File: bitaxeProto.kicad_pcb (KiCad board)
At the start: 6 copper layers, 76 x 101 mm, 242 parts, among them J1 XT30, J2 Conn_01x03, J4 Conn_01x04, J5 Conn_01x10, J6 USB_C_Receptacle_USB2.0, Q1 BSS138, SW3 SWITCH-SPST, SW4 SWITCH-SPST, U1 MCP1824T-1202E/OT, U10 TPS82130, U11 RP2040, U12 ESP32-S3-WROOM-1, U2 TPS546D24SRVFR, U3 MCP1824T-1202E/OT, U4 MCP1824T-1202E/OT, U5 W25Q16JVUXIQ TR, U6 MCP1824T-1202E/OT, U7 TPS82130, U8 SN74AXC4T774, U9 TPS22919DCKR, Y1 12MHz, Y2 50MHz

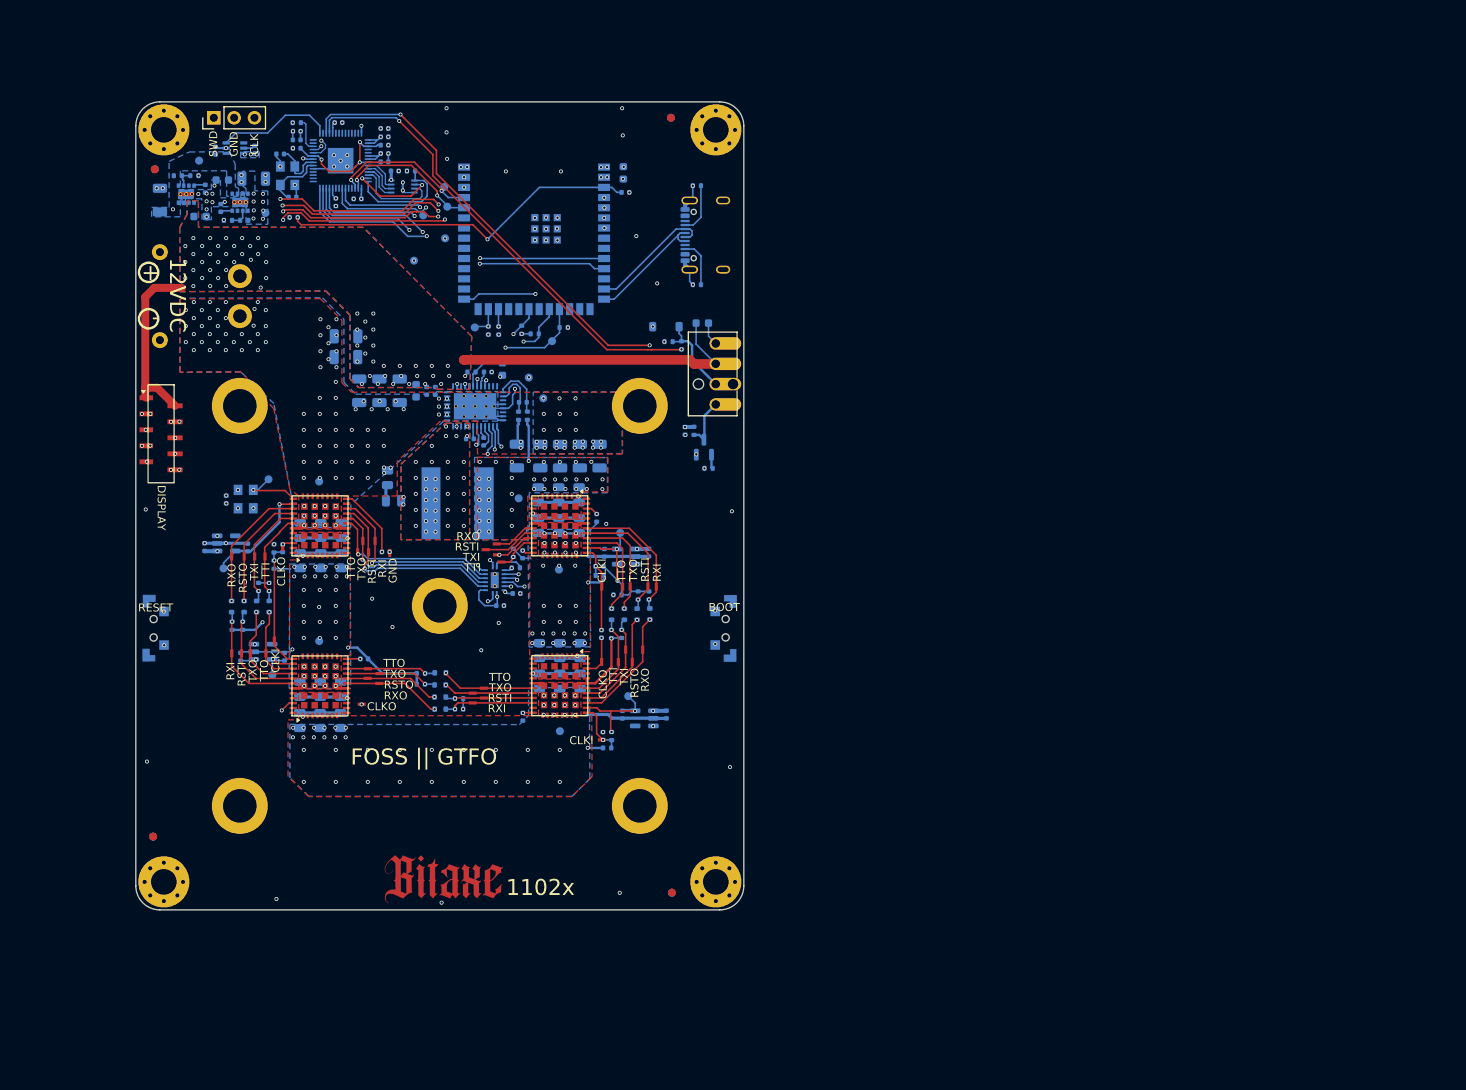
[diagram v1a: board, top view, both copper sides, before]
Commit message: add footprints and some 3d cad. rough part placements
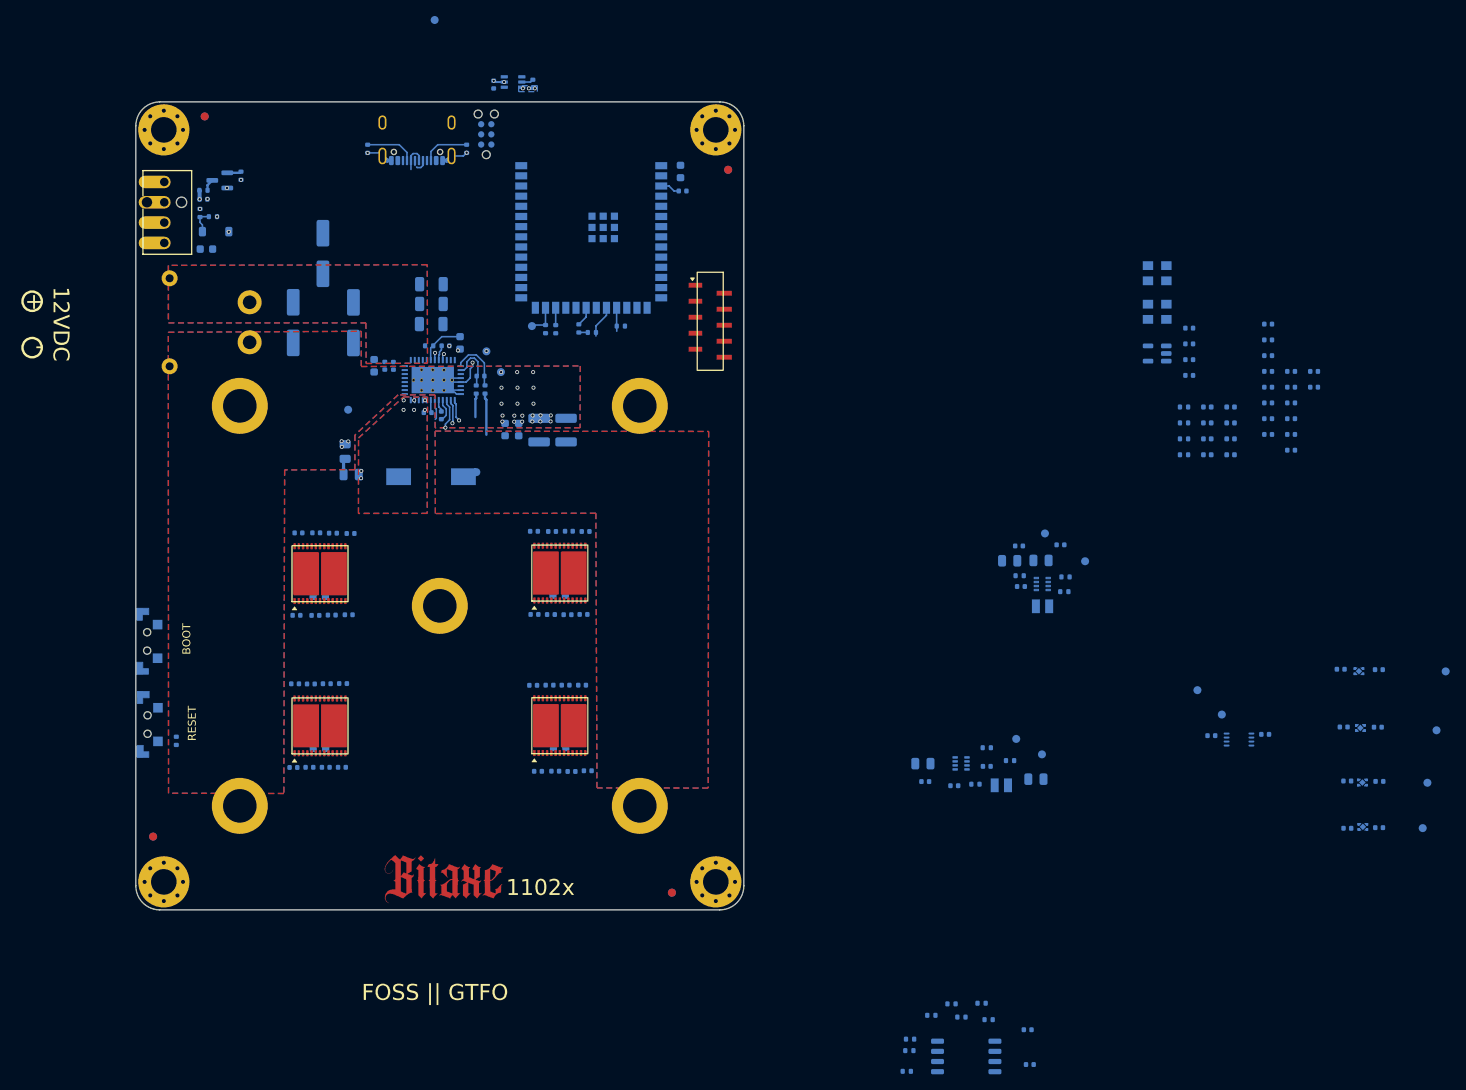
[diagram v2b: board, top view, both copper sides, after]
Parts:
- removed C132, C133, C139, C140, C141: 100uF, Capacitor_SMD:C_0805_2012Metric
- removed C142, C143, C144: 1000pF, Capacitor_SMD:C_0402_1005Metric
- removed C20: 47uF, Capacitor_SMD:C_1206_3216Metric
- removed C26, C27, C28, C39: 1uF, Capacitor_SMD:C_0402_1005Metric
- removed C31, C4, C5: 22uF, Capacitor_SMD:C_1206_3216Metric
- removed C32, C40, C43, C44, C45, C46, C58: 0.1uF, Capacitor_SMD:C_0402_1005Metric
- removed C33: 30pF, Capacitor_SMD:C_0402_1005Metric
- removed C60, C62, C63, C64: 120pF, Capacitor_SMD:C_0402_1005Metric
- removed D1, D10, D11, D12, D2, D3, D4, D5, D6, D7, D8, D9: DLLFSD01T-7, bitaxe:D_SOD-523
- removed J2: Conn_01x03, Connector_PinHeader_2.54mm:PinHeader_1x03_P2.54mm_Vertical
- removed R10: 536k, Resistor_SMD:R_0402_1005Metric
- removed R11: 100k, Resistor_SMD:R_0402_1005Metric
- removed R35, R36, R37, R38, R39, R4, R40, R41, R42, R43, R44, R45, R46, R47, R48, R49, R50, R51, R52: 1k, Resistor_SMD:R_0402_1005Metric
- removed R9: 10k, Resistor_SMD:R_0402_1005Metric
- removed TP14, TP31, TP38, TP46: RXO, bitaxe:TestPoint_Pad_1.0x0.4mm
- removed TP15: 5V, bitaxe:TestPoint_Pad_D1.0mm
- removed TP16: TXC, bitaxe:TestPoint_Pad_D1.0mm
- removed TP17, TP33, TP40, TP50, TP54: TXO, bitaxe:TestPoint_Pad_1.0x0.4mm
- removed TP18: 1V2-1, bitaxe:TestPoint_Pad_D1.0mm
- removed TP22: GND, bitaxe:TestPoint_Pad_1.0x0.4mm
- removed TP23: RXC, bitaxe:TestPoint_Pad_D1.0mm
- removed TP24: TXD, bitaxe:TestPoint_Pad_D1.0mm
- removed TP25: RXD, bitaxe:TestPoint_Pad_D1.0mm
- removed TP26: GND, bitaxe:TestPoint_Pad_D1.0mm
- removed TP28, TP43: TTI, bitaxe:TestPoint_Pad_1.0x0.4mm
- removed TP29, TP44: TXI, bitaxe:TestPoint_Pad_1.0x0.4mm
- removed TP3: 1V2-3, bitaxe:TestPoint_Pad_D1.0mm
- removed TP30, TP39, TP45: RSTO, bitaxe:TestPoint_Pad_1.0x0.4mm
- removed TP32, TP51, TP55: RSTI, bitaxe:TestPoint_Pad_1.0x0.4mm
- removed TP34, TP41, TP49, TP53: TTO, bitaxe:TestPoint_Pad_1.0x0.4mm
- removed TP35, TP48, TP57: CLKI, bitaxe:TestPoint_Pad_1.0x0.4mm
- removed TP36, TP52, TP56: RXI, bitaxe:TestPoint_Pad_1.0x0.4mm
- removed TP37, TP42, TP47: CLKO, bitaxe:TestPoint_Pad_1.0x0.4mm
- removed TP58: D1, bitaxe:TestPoint_Pad_D1.0mm
- removed TP59: D2, bitaxe:TestPoint_Pad_D1.0mm
- removed TP60: D3, bitaxe:TestPoint_Pad_D1.0mm
- removed U1, U6: MCP1824T-1202E/OT, bitaxe:SOT-23-5
- removed U10, U7: TPS82130, bitaxe:Texas_SIL0008D_MicroSiP-8-1EP_2.8x3mm_P0.65mm_EP1.1x1.9mm_ThermalVias
- removed U11: RP2040, bitaxe:RP2040-QFN-56-1EP_7x7mm_P0.4mm_EP3.2x3.2mm
- removed Y1: 12MHz, bitaxe:XTAL_ECS-120-20-33-CKM-TR3
- removed Y2: 50MHz, bitaxe:OSC_ECS-3225MV-500-CN-TR
- added C102: 1uF, Capacitor_SMD:C_0402_1005Metric, B.Cu at (118.9, 121.7)
- added C103: 1uF, Capacitor_SMD:C_0402_1005Metric, B.Cu at (116.9, 121.7)
- added C104: 1uF, Capacitor_SMD:C_0402_1005Metric, B.Cu at (114.9, 121.8)
- added C105: 1uF, Capacitor_SMD:C_0402_1005Metric, B.Cu at (112.9, 121.7)
- added C106: 1uF, Capacitor_SMD:C_0402_1005Metric, B.Cu at (142.7, 121.9)
- added C110: 1uF, Capacitor_SMD:C_0402_1005Metric, B.Cu at (143.3, 132.7)
- added C111: 1uF, Capacitor_SMD:C_0402_1005Metric, B.Cu at (145.4, 132.7)
- added C112: 1uF, Capacitor_SMD:C_0402_1005Metric, B.Cu at (147.5, 132.7)
- added C113: 1uF, Capacitor_SMD:C_0402_1005Metric, B.Cu at (149.5, 132.6)
- added C114: 1uF, Capacitor_SMD:C_0402_1005Metric, B.Cu at (113.3, 102.9)
- added C118: 1uF, Capacitor_SMD:C_0402_1005Metric, B.Cu at (113.1, 113.2)
- added C119: 1uF, Capacitor_SMD:C_0402_1005Metric, B.Cu at (115.5, 113.2)
- added C120: 1uF, Capacitor_SMD:C_0402_1005Metric, B.Cu at (117.5, 113.2)
- added C121: 1uF, Capacitor_SMD:C_0402_1005Metric, B.Cu at (119.6, 113.1)
- added C122: 1uF, Capacitor_SMD:C_0402_1005Metric, B.Cu at (142.8, 102.7)
- added C126: 1uF, Capacitor_SMD:C_0402_1005Metric, B.Cu at (142.8, 113.1)
- added C127: 1uF, Capacitor_SMD:C_0402_1005Metric, B.Cu at (144.9, 113.1)
- added C128: 1uF, Capacitor_SMD:C_0402_1005Metric, B.Cu at (147.0, 113.1)
- added C129: 1uF, Capacitor_SMD:C_0402_1005Metric, B.Cu at (149.0, 113.1)
- added C130: 0.1uF, Capacitor_SMD:C_0402_1005Metric, B.Cu at (224.7, 77.3)
- added C206: 0.1uF, Capacitor_SMD:C_0402_1005Metric, B.Cu at (204.5, 165.0)
- added C207: 1uF, Capacitor_SMD:C_0402_1005Metric, B.Cu at (204.8, 169.3)
- added C208: 0.1uF, Capacitor_SMD:C_0402_1005Metric, B.Cu at (224.7, 81.2)
- added C209: 1uF, Capacitor_SMD:C_0402_1005Metric, B.Cu at (224.7, 83.2)
- added C49: 1uF, Capacitor_SMD:C_0402_1005Metric, B.Cu at (244.0, 127.1)
- added C50: 1uF, Capacitor_SMD:C_0402_1005Metric, B.Cu at (248.4, 120.0)
- added C51: 0.1uF, Capacitor_SMD:C_0402_1005Metric, B.Cu at (240.3, 82.7)
- added C52: 0.1uF, Capacitor_SMD:C_0402_1005Metric, B.Cu at (240.3, 84.7)
- added C53: 1uF, Capacitor_SMD:C_0402_1005Metric, B.Cu at (244.4, 133.9)
- added C54: 1uF, Capacitor_SMD:C_0402_1005Metric, B.Cu at (244.4, 139.8)
- added C55: 1uF, Capacitor_SMD:C_0402_1005Metric, B.Cu at (248.2, 127.2)
- added C56: 1uF, Capacitor_SMD:C_0402_1005Metric, B.Cu at (248.4, 133.9)
- added C66: 10uF, Capacitor_SMD:C_0603_1608Metric, B.Cu at (146.0, 125.0)
- added C67: 10uF, Capacitor_SMD:C_0603_1608Metric, B.Cu at (146.0, 126.6)
- added C69: 10uF, Capacitor_SMD:C_0603_1608Metric, B.Cu at (146.0, 129.7)
- added C70: 10uF, Capacitor_SMD:C_0603_1608Metric, B.Cu at (146.0, 105.9)
- added C71: 10uF, Capacitor_SMD:C_0603_1608Metric, B.Cu at (146.0, 107.5)
- added C73: 10uF, Capacitor_SMD:C_0603_1608Metric, B.Cu at (116.0, 125.1)
- added C74: 10uF, Capacitor_SMD:C_0603_1608Metric, B.Cu at (116.0, 126.7)
- added C75: 10uF, Capacitor_SMD:C_0603_1608Metric, B.Cu at (116.0, 128.2)
- added C78: 10uF, Capacitor_SMD:C_0603_1608Metric, B.Cu at (116.0, 129.8)
- added C79: 4.7uF, Capacitor_SMD:C_0402_1005Metric, B.Cu at (237.4, 84.7)
- added C80: 10uF, Capacitor_SMD:C_0603_1608Metric, B.Cu at (116.0, 106.0)
- added C81: 10uF, Capacitor_SMD:C_0603_1608Metric, B.Cu at (116.0, 107.6)
- added C82: 10uF, Capacitor_SMD:C_0603_1608Metric, B.Cu at (116.0, 109.2)
- added C86: 0.1uF, Capacitor_SMD:C_0402_1005Metric, B.Cu at (237.4, 90.6)
- added C87: 4.7uF, Capacitor_SMD:C_0402_1005Metric, B.Cu at (237.4, 92.5)
- added C88: 0.1uF, Capacitor_SMD:C_0402_1005Metric, B.Cu at (234.5, 76.8)
- added C89: 4.7uF, Capacitor_SMD:C_0402_1005Metric, B.Cu at (234.5, 78.8)
- added C90: 0.1uF, Capacitor_SMD:C_0402_1005Metric, B.Cu at (234.5, 80.7)
- added C94: 4.7uF, Capacitor_SMD:C_0402_1005Metric, B.Cu at (234.5, 86.6)
- added C95: 10uF, Capacitor_SMD:C_0603_1608Metric, B.Cu at (145.9, 110.7)
- added C96: 0.1uF, Capacitor_SMD:C_0402_1005Metric, B.Cu at (234.5, 88.6)
- added C97: 4.7uF, Capacitor_SMD:C_0402_1005Metric, B.Cu at (234.5, 90.6)
- added C98: 1uF, Capacitor_SMD:C_0402_1005Metric, B.Cu at (112.7, 132.2)
- added FB10: FerriteBead_Small, Inductor_SMD:L_0402_1005Metric, B.Cu at (226.9, 93.1)
- added FB3: FerriteBead_Small, Inductor_SMD:L_0402_1005Metric, B.Cu at (229.8, 87.1)
- added FB4: FerriteBead_Small, Inductor_SMD:L_0402_1005Metric, B.Cu at (229.8, 89.1)
- added FB5: FerriteBead_Small, Inductor_SMD:L_0402_1005Metric, B.Cu at (229.8, 91.1)
- added FB6: FerriteBead_Small, Inductor_SMD:L_0402_1005Metric, B.Cu at (229.8, 93.1)
- added FB7: FerriteBead_Small, Inductor_SMD:L_0402_1005Metric, B.Cu at (226.9, 87.1)
- added FB8: FerriteBead_Small, Inductor_SMD:L_0402_1005Metric, B.Cu at (226.9, 89.1)
- added FB9: FerriteBead_Small, Inductor_SMD:L_0402_1005Metric, B.Cu at (226.9, 91.1)
- added J8: TC2030-IDC, Connector:Tag-Connect_TC2030-IDC-NL_2x03_P1.27mm_Vertical, B.Cu at (136.8, 53.1)
- added L2: 1.5uH, bitaxe:IND-SMD_L2.0-W1.6, B.Cu at (206.3, 112.0)
- added L3: 1.5uH, bitaxe:IND-SMD_L2.0-W1.6, B.Cu at (201.2, 134.4)
- added R15: 10k, Resistor_SMD:R_0402_1005Metric, B.Cu at (197.9, 134.3)
- added R25: 10k, Resistor_SMD:R_0402_1005Metric, B.Cu at (224.0, 87.1)
- added R27: 10k, Resistor_SMD:R_0402_1005Metric, B.Cu at (202.3, 131.3)
- added R55: 1k, Resistor_SMD:R_0402_1005Metric, B.Cu at (198.7, 161.7)
- added R56: 10k, Resistor_SMD:R_0402_1005Metric, B.Cu at (195.0, 161.8)
- added R57: 10k, Resistor_SMD:R_0402_1005Metric, B.Cu at (192.4, 163.2)
- added R58: 1k, Resistor_SMD:R_0402_1005Metric, B.Cu at (189.4, 170.2)
- added R59: 10k, Resistor_SMD:R_0402_1005Metric, B.Cu at (189.7, 167.6)
- added R60: 10k, Resistor_SMD:R_0402_1005Metric, B.Cu at (189.8, 166.2)
- added R68: 1k, Resistor_SMD:R_0402_1005Metric, B.Cu at (199.6, 163.7)
- added R69: 1k, Resistor_SMD:R_0402_1005Metric, B.Cu at (196.2, 163.4)
- added R70: 220k, Resistor_SMD:R_0402_1005Metric, B.Cu at (224.0, 91.1)
- added R71: 1k, Resistor_SMD:R_0402_1005Metric, B.Cu at (224.0, 93.1)
- added U13: TS3011, bitaxe:SOT-23-5, B.Cu at (220.7, 80.5)
- added U14: SN74AVC2T45DCUR, bitaxe:VSSOP-8_L2.1-W2.4-P0.50-LS3.2-BR, B.Cu at (230.9, 128.7)
- added U15: 25MHz, bitaxe:SMD3225-4P, B.Cu at (220.7, 75.2)
- added U16: TLV75512PDQNR, bitaxe:DQN0004A, B.Cu at (246.1, 127.3)
- added U17: TLV755075PDQNR, bitaxe:DQN0004A, B.Cu at (246.3, 134.1)
- added U18: TLV75512PDQNR, bitaxe:DQN0004A, B.Cu at (246.4, 139.6)
- added U19: TLV3542, Package_SO:SOIC-8_5.3x5.3mm_P1.27mm, B.Cu at (196.8, 168.3)
- A1, A3: value BZM2_MODE0 -> ProtoMC3; footprint bitaxe:bzm2 -> bitaxe:proto-mc3
- A2, A4: value BZM2_MODE1 -> ProtoMC3; footprint bitaxe:bzm2 -> bitaxe:proto-mc3
- C1: value 10uF -> 68uF; footprint Capacitor_SMD:C_0603_1608Metric -> Capacitor_SMD:C_Elec_6.3x7.7
- C100, C101, C107, C108, C109, C115, C116, C117, C123, C124, C125, C99: value 100uF -> 1uF; footprint Capacitor_SMD:C_0805_2012Metric -> Capacitor_SMD:C_0402_1005Metric
- C12: value 3.3nF -> 10uF; footprint Capacitor_SMD:C_0402_1005Metric -> Capacitor_SMD:C_0805_2012Metric
- C131, C85, C92: value 100uF -> 4.7uF; footprint Capacitor_SMD:C_0805_2012Metric -> Capacitor_SMD:C_0402_1005Metric
- C19, C7: value 1uF -> 4.7uF; footprint Capacitor_SMD:C_0402_1005Metric -> Capacitor_SMD:C_1206_3216Metric
- C2, C3: value 22uF -> 68uF; footprint Capacitor_SMD:C_1206_3216Metric -> Capacitor_SMD:C_Elec_6.3x7.7
- C21, C22: value 100uF -> 22uF; footprint Capacitor_SMD:C_1206_3216Metric -> Capacitor_SMD:C_0603_1608Metric
- C23, C24: footprint Capacitor_SMD:C_1206_3216Metric -> Capacitor_SMD:C_1210_3225Metric
- C29: value 3.3nF -> 33nF
- C30: value 22uF -> 33nF; footprint Capacitor_SMD:C_1206_3216Metric -> Capacitor_SMD:C_0402_1005Metric
- C35: value 30pF -> 22uF; footprint Capacitor_SMD:C_0402_1005Metric -> Capacitor_SMD:C_0805_2012Metric
- C36: value 0.1uF -> 22uF; footprint Capacitor_SMD:C_0402_1005Metric -> Capacitor_SMD:C_0805_2012Metric
- C38, C72: value 1uF -> 0.1uF
- C57: value 0.1uF -> 1uF
- C6: value 22uF -> 4.7uF
- C61: value 120pF -> 0.1uF
- C68: value 1uF -> 10uF; footprint Capacitor_SMD:C_0402_1005Metric -> Capacitor_SMD:C_0603_1608Metric
- C8: footprint Capacitor_SMD:C_0603_1608Metric -> Capacitor_SMD:C_0805_2012Metric
- C83, C93: value 100uF -> 10uF; footprint Capacitor_SMD:C_0805_2012Metric -> Capacitor_SMD:C_0603_1608Metric
- C84, C91: value 100uF -> 0.1uF; footprint Capacitor_SMD:C_0805_2012Metric -> Capacitor_SMD:C_0402_1005Metric
- L1: value 1.2uH -> 230nH; footprint bitaxe:XAL1060122MEC -> bitaxe:IND-SMD_L11.0-W7.2
- R12: value 309k -> 30.9k
- R13: value 100k -> 10k
- R14: value 10k -> 13.7k
- R16: value 49.9k -> 52.3k
- R26: value 20k -> 12k
- TP11: value TTI -> CLKI; footprint bitaxe:TestPoint_Pad_1.0x0.4mm -> bitaxe:TestPoint_Pad_D1.0mm; moved to B.Cu
- TP12: value TXI -> 1V2; footprint bitaxe:TestPoint_Pad_1.0x0.4mm -> bitaxe:TestPoint_Pad_D1.0mm; moved to B.Cu
- TP13: value RSTI -> 5V; footprint bitaxe:TestPoint_Pad_1.0x0.4mm -> bitaxe:TestPoint_Pad_D1.0mm; moved to B.Cu
- TP2: value 1V2-2 -> 0V75-0
- TP20: value RXI -> GND; footprint bitaxe:TestPoint_Pad_1.0x0.4mm -> bitaxe:TestPoint_Pad_D1.0mm; moved to B.Cu
- TP21: value TTO -> GND; footprint bitaxe:TestPoint_Pad_1.0x0.4mm -> bitaxe:TestPoint_Pad_D1.0mm; moved to B.Cu
- TP4: value 1V2-4 -> 1V2-0
- TP5, TP8: footprint TestPoint:TestPoint_Pad_D1.0mm -> bitaxe:TestPoint_Pad_D1.0mm
- TP6: value RSTI -> 0V75; footprint bitaxe:TestPoint_Pad_1.0x0.4mm -> bitaxe:TestPoint_Pad_D1.0mm; moved to B.Cu
- U3: value MCP1824T-1202E/OT -> TLV755075PDQNR; footprint bitaxe:SOT-23-5 -> bitaxe:DQN0004A
- U4: value MCP1824T-1202E/OT -> TPS62933DRLR; footprint bitaxe:SOT-23-5 -> bitaxe:SOT-583-8_L2.1-W1.2-P0.50-LS1.6-BR
- U5: value W25Q16JVUXIQ TR -> TPS62933DRLR; footprint bitaxe:USON-8_UX_2x3x0p6_WIN -> bitaxe:SOT-583-8_L2.1-W1.2-P0.50-LS1.6-BR
- U8: value SN74AXC4T774 -> 25MHz; footprint bitaxe:BQB0016A-MFG -> bitaxe:SMD3225-4P
- moved TP2 146.7 mm to (256.7, 120.2), turned to 180 degrees
- moved TP6 135.5 mm to (254.4, 134.1), turned to 180 degrees
- moved C72 132.3 mm to (237.4, 82.7), turned to 180 degrees
- moved C30 123.4 mm to (195.3, 134.5), turned to 180 degrees
- moved C84 122.9 mm to (237.4, 86.6), turned to 180 degrees
- moved TP10 122.7 mm to (228.8, 125.6), turned to 180 degrees
- moved C91 122.6 mm to (234.5, 82.7), turned to 180 degrees
- moved TP12 120.6 mm to (253.9, 139.8), turned to 180 degrees
- moved C85 120.0 mm to (237.4, 88.6), turned to 180 degrees
- moved C92 119.8 mm to (234.5, 84.7), turned to 180 degrees
- moved C42 117.2 mm to (199.4, 132.1), turned to 180 degrees
- moved R16 116.4 mm to (199.4, 129.7)
- moved C12 114.9 mm to (191.4, 131.7), turned to 180 degrees
- moved R13 114.4 mm to (209.1, 110.2), turned to 180 degrees
- moved C57 113.3 mm to (248.4, 139.7), turned to 180 degrees
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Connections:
- A1 pad 1: /ASIC/bypass1-1/out -> Net-(A1-CLKO)
- A1 pad 10: unconnected-(A1-TDI-Pad10) -> GND
- A1 pad 11: unconnected-(A1-TCK-Pad11) -> Net-(A1-VDDI1_0)
- A1 pad 12: /ASIC/bypass1-2/in -> Net-(A1-VDDI2_0)
- A1 pad 13: unconnected-(A1-RSVD-Pad13) -> Net-(A1-VDDI3_0)
- A1 pad 14: GND -> Net-(A1-VDDI3_1)
- A1 pad 15: /ASIC/TRIP_1V2 -> Net-(A1-VDDI2_1)
- A1 pad 16: /ASIC/TX_1V2 -> Net-(A1-VDDI1_1)
- A1 pad 17: /ASIC/RST_1V2 -> GND
- A1 pad 18: /ASIC/RX_1V2 -> unconnected-(A1-VEFS-Pad18)
- A1 pad 19: unconnected-(A1-VDDIO-Pad19) -> /ASIC/RST_1V2
- A1 pad 2: /ASIC/GND2 -> unconnected-(A1-UTXN-Pad2)
- A1 pad 20: Net-(A1-REFCLKOUT2) -> unconnected-(A1-TO-Pad20)
- A1 pad 21: GND -> Net-(A1-VDDIO12-Pad21)
- A1 pad 22: GND -> Net-(A1-VDDH-Pad22)
- A1 pad 24: GND -> /ASIC/RX_1V2
- A1 pad 25: GND -> unconnected-(A1-URXN-Pad25)
- A1 pad 26: GND -> /ASIC/CLKI
- A1 pad 28: GND -> /ASIC/GND0
- A1 pad 3: /ASIC/GND2 -> Net-(A1-UTXP)
- A1 pad 4: /ASIC/GND2 -> unconnected-(A1-ATEST-Pad4)
- A1 pad 5: /ASIC/GND2 -> Net-(A1-VDDH-Pad22)
- A1 pad 6: /ASIC/GND2 -> Net-(A1-VDDIO12-Pad21)
- A1 pad 7: /ASIC/GND2 -> Net-(A1-nRST-Pad7)
- A1 pad 8: /ASIC/GND2 -> GND
- A1 pad 9: unconnected-(A1-TDO-Pad9) -> GND
- A2 pad 1: /ASIC/bypass2-1/out -> unconnected-(A2-CLKO-Pad1)
- A2 pad 10: unconnected-(A2-TDI-Pad10) -> GND
- A2 pad 11: unconnected-(A2-TCK-Pad11) -> Net-(A2-VDDI1_0)
- A2 pad 12: /ASIC/bypass2-2/in -> Net-(A2-VDDI2_0)
- A2 pad 13: unconnected-(A2-RSVD-Pad13) -> Net-(A2-VDDI3_0)
- A2 pad 14: /ASIC/GND2 -> Net-(A2-VDDI3_1)
- A2 pad 15: /ASIC/shifter2-3/RX_OUT -> Net-(A2-VDDI2_1)
- A2 pad 16: /ASIC/shifter2-3/RESET_OUT -> Net-(A2-VDDI1_1)
- A2 pad 17: /ASIC/shifter2-3/TX_IN -> GND
- A2 pad 18: /ASIC/shifter2-3/TRIP_IN -> unconnected-(A2-VEFS-Pad18)
- A2 pad 19: unconnected-(A2-VDDIO-Pad19) -> Net-(A1-nRST-Pad7)
- A2 pad 2: /ASIC/GND3 -> unconnected-(A2-UTXN-Pad2)
- A2 pad 20: Net-(A2-REFCLKOUT2) -> unconnected-(A2-TO-Pad20)
- A2 pad 21: /ASIC/GND2 -> /ASIC/1V2
- A2 pad 22: /ASIC/GND2 -> /ASIC/0V75
- A2 pad 23: /ASIC/GND2 -> GND
- A2 pad 24: /ASIC/GND2 -> Net-(A1-UTXP)
- A2 pad 25: /ASIC/GND2 -> unconnected-(A2-URXN-Pad25)
- A2 pad 26: /ASIC/GND2 -> Net-(A1-CLKO)
- A2 pad 27: /ASIC/GND2 -> GND
- A2 pad 28: /ASIC/GND2 -> /ASIC/GND0
- A2 pad 3: /ASIC/GND3 -> /ASIC/Level Shifter/TX_IN
- A2 pad 4: /ASIC/GND3 -> unconnected-(A2-ATEST-Pad4)
- A2 pad 5: /ASIC/GND3 -> /ASIC/0V75
- A2 pad 6: /ASIC/GND3 -> /ASIC/1V2
- A2 pad 7: /ASIC/GND3 -> /ASIC/Level Shifter/RST_IN
- A2 pad 8: /ASIC/GND3 -> GND
- A2 pad 9: unconnected-(A2-TDO-Pad9) -> GND
- A3 pad 1: /ASIC/bypass3-1/out -> /ASIC/CLKI-0
- A3 pad 10: unconnected-(A3-TDI-Pad10) -> /ASIC/GND0
- A3 pad 11: unconnected-(A3-TCK-Pad11) -> Net-(A3-VDDI1_0)
- A3 pad 12: /ASIC/bypass3-2/in -> Net-(A3-VDDI2_0)
- A3 pad 13: unconnected-(A3-RSVD-Pad13) -> Net-(A3-VDDI3_0)
- A3 pad 14: /ASIC/GND3 -> Net-(A3-VDDI3_1)
- A3 pad 15: /ASIC/shifter2-3/TRIP_OUT -> Net-(A3-VDDI2_1)
- A3 pad 16: /ASIC/shifter2-3/TX_OUT -> Net-(A3-VDDI1_1)
- A3 pad 17: /ASIC/shifter2-3/RESET_IN -> /ASIC/GND0
- A3 pad 18: /ASIC/shifter2-3/RX_IN -> unconnected-(A3-VEFS-Pad18)
- A3 pad 19: unconnected-(A3-VDDIO-Pad19) -> Net-(A3-nRST-Pad19)
- A3 pad 2: /ASIC/GND4 -> unconnected-(A3-URXN-Pad2)
- A3 pad 20: Net-(A3-REFCLKOUT2) -> unconnected-(A3-TO-Pad20)
- A3 pad 21: /ASIC/GND3 -> /ASIC/1V2-0
- A3 pad 22: /ASIC/GND3 -> /ASIC/0V75-0
- A3 pad 23: /ASIC/GND3 -> /ASIC/GND0
- A3 pad 24: /ASIC/GND3 -> Net-(A3-UTXP)
- A3 pad 25: /ASIC/GND3 -> unconnected-(A3-UTXN-Pad25)
- A3 pad 26: /ASIC/GND3 -> Net-(A3-CLKO)
- A3 pad 27: /ASIC/GND3 -> /ASIC/GND0
- A3 pad 28: /ASIC/GND3 -> /VDD
- A3 pad 3: /ASIC/GND4 -> /ASIC/Level Shifter/TX_OUT
- A3 pad 4: /ASIC/GND4 -> unconnected-(A3-ATEST-Pad4)
- A3 pad 5: /ASIC/GND4 -> /ASIC/0V75-0
- A3 pad 6: /ASIC/GND4 -> /ASIC/1V2-0
- A3 pad 7: /ASIC/GND4 -> /ASIC/Level Shifter/RST_OUT
- A3 pad 8: /ASIC/GND4 -> /ASIC/1V2-0
- A3 pad 9: unconnected-(A3-TDO-Pad9) -> /ASIC/GND0
- A4 pad 1: /ASIC/bypass4-1/out -> Net-(A3-CLKO)
- A4 pad 10: unconnected-(A4-TDI-Pad10) -> /ASIC/GND0
- A4 pad 11: unconnected-(A4-TCK-Pad11) -> Net-(A4-VDDI1_0)
- A4 pad 12: /ASIC/bypass4-2/in -> Net-(A4-VDDI2_0)
- A4 pad 13: unconnected-(A4-RSVD-Pad13) -> Net-(A4-VDDI3_0)
- A4 pad 14: /ASIC/GND4 -> Net-(A4-VDDI3_1)
- A4 pad 15: Net-(A4-RX_OUT) -> Net-(A4-VDDI2_1)
- A4 pad 16: Net-(A4-RESET_OUT) -> Net-(A4-VDDI1_1)
- A4 pad 17: Net-(A4-TX_IN) -> /ASIC/GND0
- A4 pad 18: Net-(A4-TRIP_IN) -> unconnected-(A4-VEFS-Pad18)
- A4 pad 2: /VDD -> unconnected-(A4-URXN-Pad2)
- A4 pad 20: Net-(A4-REFCLKOUT2) -> unconnected-(A4-TO-Pad20)
- A4 pad 21: /ASIC/GND4 -> Net-(A4-VDDIO12-Pad21)
- A4 pad 22: /ASIC/GND4 -> Net-(A4-VDDH-Pad22)
- A4 pad 23: /ASIC/GND4 -> /ASIC/GND0
- A4 pad 24: /ASIC/GND4 -> /ASIC/TX_2V4
- A4 pad 25: /ASIC/GND4 -> unconnected-(A4-UTXN-Pad25)
- A4 pad 26: /ASIC/GND4 -> unconnected-(A4-CLKO-Pad26)
- A4 pad 27: /ASIC/GND4 -> /ASIC/GND0
- A4 pad 28: /ASIC/GND4 -> /VDD
- A4 pad 3: /VDD -> Net-(A3-UTXP)
- A4 pad 4: /VDD -> unconnected-(A4-ATEST-Pad4)
- A4 pad 5: /VDD -> Net-(A4-VDDH-Pad22)
- A4 pad 6: /VDD -> Net-(A4-VDDIO12-Pad21)
- A4 pad 7: /VDD -> Net-(A3-nRST-Pad19)
- A4 pad 8: /VDD -> /ASIC/1V2-0
- A4 pad 9: unconnected-(A4-TDO-Pad9) -> /ASIC/GND0
- C1 pad 1: GND -> /12V
- C1 pad 2: /12V -> GND
- C100 pad 1: /ASIC/bypass2-1/out -> Net-(A2-VDDI2_0)
- C100 pad 2: /ASIC/GND3 -> Net-(A2-VDDI1_0)
- C101 pad 1: /ASIC/bypass2-1/out -> Net-(A2-VDDI1_0)
- C101 pad 2: /ASIC/GND3 -> GND
- C107 pad 1: /ASIC/GND2 -> Net-(A3-VDDI2_1)
- C107 pad 2: /ASIC/bypass2-2/in -> Net-(A3-VDDI1_1)
- C108 pad 1: /ASIC/GND2 -> Net-(A3-VDDI3_1)
- C108 pad 2: /ASIC/bypass2-2/in -> Net-(A3-VDDI2_1)
- C109 pad 1: /ASIC/GND2 -> /VDD
- C109 pad 2: /ASIC/bypass2-2/in -> Net-(A3-VDDI3_1)
- C115 pad 1: /ASIC/bypass3-1/out -> Net-(A1-VDDI2_1)
- C115 pad 2: /ASIC/GND4 -> Net-(A1-VDDI1_1)
- C116 pad 1: /ASIC/bypass3-1/out -> Net-(A1-VDDI3_1)
- C116 pad 2: /ASIC/GND4 -> Net-(A1-VDDI2_1)
- C117 pad 1: /ASIC/bypass3-1/out -> /ASIC/GND0
- C117 pad 2: /ASIC/GND4 -> Net-(A1-VDDI3_1)
- C12 pad 2: Net-(U7-SS/TR) -> /12V
- C123 pad 1: /ASIC/GND3 -> Net-(A4-VDDI2_1)
- C123 pad 2: /ASIC/bypass3-2/in -> Net-(A4-VDDI1_1)
- C124 pad 1: /ASIC/GND3 -> Net-(A4-VDDI3_1)
- C124 pad 2: /ASIC/bypass3-2/in -> Net-(A4-VDDI2_1)
- C125 pad 1: /ASIC/GND3 -> /VDD
- C125 pad 2: /ASIC/bypass3-2/in -> Net-(A4-VDDI3_1)
- C131 pad 1: /ASIC/bypass4-1/out -> /ASIC/GND0
- C131 pad 2: /VDD -> /ASIC/1V2-0
- C19 pad 1: /ASIC/GND2 -> /12V
- C19 pad 2: /ASIC/1V2-2 -> GND
- C25 pad 1: /ASIC/GND3 -> /ASIC/GND0
- C29 pad 2: Net-(U10-SS/TR) -> Net-(U4-SS)
- C30 pad 2: /5V -> Net-(U5-SS)
- C35 pad 2: /Data/XIN -> /3V3
- C36 pad 2: /Data/1V1 -> /5V
- C37 pad 1: GND -> /12V
- C37 pad 2: /Data/1V1 -> GND
- C38 pad 1: GND -> /12V
- C38 pad 2: /Data/1V1 -> GND
- C41 pad 1: GND -> Net-(U4-BST)
- C41 pad 2: /3V3 -> Net-(U4-SW)
- C42 pad 1: GND -> Net-(U5-BST)
- C42 pad 2: /3V3 -> Net-(U5-SW)
- C57 pad 1: /ASIC/1V2-1 -> GND
- C57 pad 2: GND -> /ASIC/1V2
- C59 pad 1: /3V3 -> /ASIC/1V2
- C59 pad 2: GND -> Net-(U14-GND)
- C61 pad 1: Net-(A4-REFCLKOUT2) -> /3V3
- C61 pad 2: /ASIC/GND4 -> Net-(U14-GND)
- C68 pad 1: GND -> /VDD
- C68 pad 2: /5V_SWITCH -> /ASIC/GND0
- C7 pad 1: /ASIC/GND2 -> /12V
- C7 pad 2: /5V_SWITCH -> GND
- C72 pad 2: /ASIC/1V2-1 -> /ASIC/0V75
- C8 pad 2: /5V -> /12V
- C83 pad 1: /ASIC/bypass1-1/out -> /ASIC/GND0
- C83 pad 2: /ASIC/GND2 -> GND
- C84 pad 1: /ASIC/bypass1-1/out -> GND
- C84 pad 2: /ASIC/GND2 -> /ASIC/0V75
- C85 pad 1: /ASIC/bypass1-1/out -> GND
- C85 pad 2: /ASIC/GND2 -> /ASIC/0V75
- C91 pad 2: /ASIC/bypass1-2/in -> /ASIC/1V2
- C92 pad 1: GND -> /ASIC/GND0
- C92 pad 2: /ASIC/bypass1-2/in -> /ASIC/1V2-0
- C93 pad 1: GND -> /VDD
- C93 pad 2: /ASIC/bypass1-2/in -> /ASIC/GND0
- C99 pad 1: /ASIC/bypass2-1/out -> Net-(A2-VDDI3_0)
- C99 pad 2: /ASIC/GND3 -> Net-(A2-VDDI2_0)
- R12 pad 1: Net-(U10-FB) -> Net-(U4-FB)
- R13 pad 2: Net-(U10-FB) -> Net-(U4-FB)
- R14 pad 1: /3V3 -> GND
- R14 pad 2: /Data/QSPI_SS -> Net-(U4-RT)
- R16 pad 1: Net-(U11-RUN) -> Net-(U5-FB)
- R16 pad 2: /3V3 -> /5V
- R26 pad 2: Net-(U8-OE) -> Net-(U13--)
- TP10 pad 1: /ASIC/REFCLKIN1 -> /ASIC/CLKI
- TP11 pad 1: Net-(A4-TRIP_IN) -> /ASIC/CLKI-0
- TP12 pad 1: Net-(A4-TX_IN) -> /ASIC/1V2
- TP13 pad 1: Net-(A4-RESET_OUT) -> /5V
- TP2 pad 1: /ASIC/1V2-2 -> /ASIC/0V75-0
- TP20 pad 1: /ASIC/RX_1V2 -> GND
- TP21 pad 1: /ASIC/TRIP_1V2 -> GND
- TP4 pad 1: /ASIC/1V2-4 -> /ASIC/1V2-0
- TP6 pad 1: /ASIC/RST_1V2 -> /ASIC/0V75
- U12 pad 10: /Data/ESP32_TX_DATA -> /ASIC/RX_3V3
- U12 pad 11: /Data/ESP32_RX_DATA -> /ASIC/TX_3V3
- U12 pad 12: unconnected-(U12-GPIO8/TOUCH8/ADC1_CH7/SUBSPICS1-Pad12) -> /Data/FAN_PWM
- U12 pad 17: unconnected-(U12-GPIO9/TOUCH9/ADC1_CH8/FSPIHD/SUBSPIHD-Pad17) -> /Data/FAN_TACH
- U12 pad 36: /Data/ESP32_RX_CTRL -> /Data/P_RX
- U12 pad 37: /Data/ESP32_TX_CTRL -> /Data/P_TX
- U12 pad 38: /Data/SWD -> unconnected-(U12-GPIO2/TOUCH2/ADC1_CH1-Pad38)
- U12 pad 39: /Data/SWCLK -> /Data/ASIC_RST
- U3 pad 1: /5V_SWITCH -> /ASIC/0V75-0
- U3 pad 2: /ASIC/GND3 -> /ASIC/GND0
- U3 pad 4: unconnected-(U3-PG-Pad4) -> /5V_SWITCH
- U3 pad 5: /ASIC/1V2-3 -> /ASIC/GND0
- U4 pad 1: /5V_SWITCH -> Net-(U4-RT)
- U4 pad 2: /ASIC/GND4 -> unconnected-(U4-EN-Pad2)
- U4 pad 3: /5V_SWITCH -> /12V
- U4 pad 4: unconnected-(U4-PG-Pad4) -> GND
- U4 pad 5: /ASIC/1V2-4 -> Net-(U4-SW)
- U5 pad 1: /Data/QSPI_SS -> Net-(U5-RT)
- U5 pad 2: /Data/QSPI_SD1 -> unconnected-(U5-EN-Pad2)
- U5 pad 3: /Data/QSPI_SD2 -> /12V
- U5 pad 5: /Data/QSPI_SD0 -> Net-(U5-SW)
- U5 pad 6: /Data/QSPI_SCLK -> Net-(U5-BST)
- U5 pad 7: /Data/QSPI_SD3 -> Net-(U5-SS)
- U5 pad 8: /3V3 -> Net-(U5-FB)
- U8 pad 1: GND -> /ASIC/1V2
- U8 pad 2: /ASIC/1V2-1 -> GND
- U8 pad 3: /ASIC/RST_1V2 -> /ASIC/CLKI
- U8 pad 4: /ASIC/TX_1V2 -> /ASIC/1V2
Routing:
- net /5V_SWITCH: track 182.4 -> 0.00 mm, vias 11 -> 3
- net /Data/EN: track 109.8 -> 2.45 mm, vias 3 -> 0
- net /Data/DISP_GPIO1: track 90.9 -> 0.00 mm, vias 4 -> 0
- net /Data/DISP_SDA: track 90.4 -> 0.00 mm, vias 4 -> 0
- net /ASIC/TX_3V3: track 88.5 -> 0.00 mm, vias 2 -> 0
- net /ASIC/RST_3V3: track 88.5 -> 0.00 mm, vias 2 -> 0
- net /Data/DISP_SCL: track 87.3 -> 0.00 mm, vias 4 -> 0
- net /Data/DISP_GPIO2: track 87.0 -> 0.00 mm, vias 4 -> 0
- net /ASIC/RX_3V3: track 86.2 -> 0.00 mm, vias 2 -> 0
- net /ASIC/TRIP_3V3: track 84.9 -> 0.00 mm, vias 2 -> 0
- net /5V: track 78.6 -> 1.13 mm, vias 2 -> 1
- net /Data/FAN_PWM: track 75.6 -> 0.01 mm, vias 3 -> 1
- net /ASIC/1V2-1: track 64.5 -> 0.00 mm, vias 6 -> 0
- net /3V3: track 64.5 -> 1.27 mm, vias 32 -> 1
- net /Data/IO0: track 62.4 -> 0.00 mm, vias 2 -> 0
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- removed copper zone on B.Cu, net /3V3
- removed copper zone on In2.Cu, net /3V3
- removed copper zone on B.Cu, net /5V
- removed copper zone on B.Cu, net /ASIC/GND2
- removed copper zone on F.Cu, net /ASIC/GND2
- removed copper zone on In2.Cu, net /ASIC/GND2
- removed copper zone on B.Cu, net /ASIC/GND3
- removed copper zone on F.Cu, net /ASIC/GND3
- removed copper zone on In2.Cu, net /ASIC/GND3
- removed copper zone on B.Cu, net /ASIC/GND4
- removed copper zone on F.Cu, net /ASIC/GND4
- removed copper zone on In2.Cu, net /ASIC/GND4
- removed copper zone on In2.Cu, net /VDD
- removed copper zone on In2.Cu, net GND
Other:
- board text removed: "CLK"
- board text removed: "DISPLAY"
- board text removed: "GND"
- board text removed: "SWD"

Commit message: a lot more rough component placement
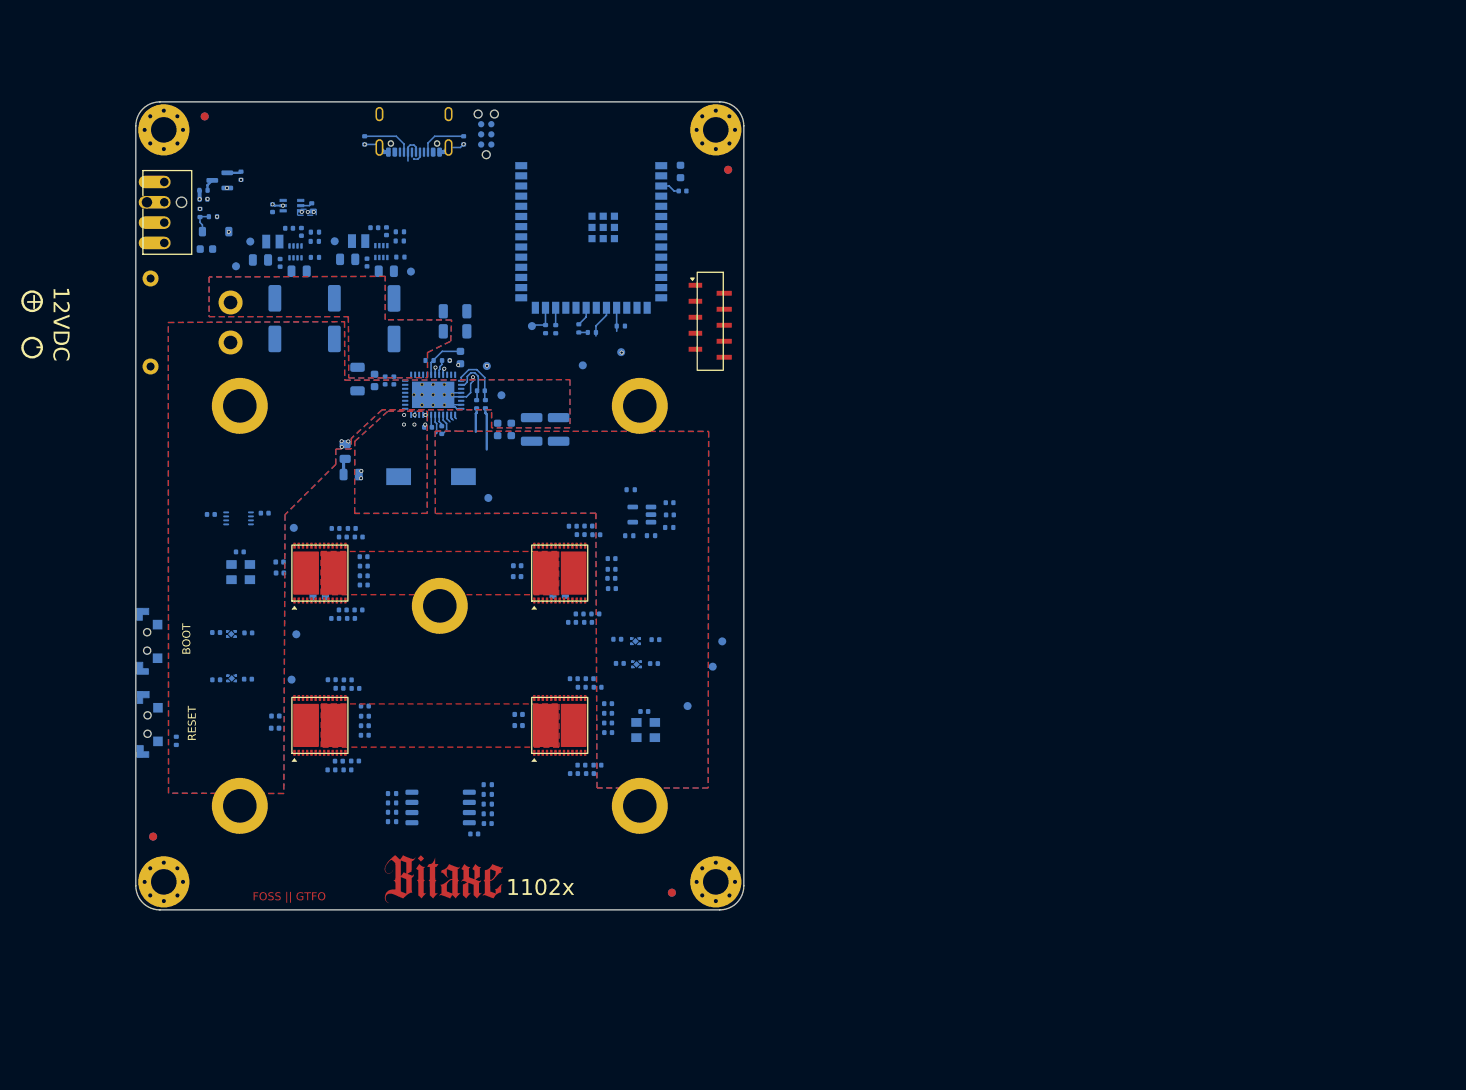
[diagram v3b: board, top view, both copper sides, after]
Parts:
- moved TP12 142.6 mm to (112.5, 121.2)
- moved C53 142.6 mm to (103.0, 115.3)
- moved C54 142.6 mm to (103.0, 121.2)
- moved C56 142.6 mm to (107.1, 115.4)
- moved C57 142.6 mm to (107.0, 121.2)
- moved TP6 142.6 mm to (113.1, 115.5)
- moved U17 142.6 mm to (104.9, 115.5)
- moved U18 142.6 mm to (105.0, 121.1)
- moved C51 136.2 mm to (106.0, 105.3), turned to 0 degrees
- moved C59 128.1 mm to (109.1, 100.4)
- moved C61 128.1 mm to (102.4, 100.6)
- moved U14 128.1 mm to (105.8, 101.1)
- moved FB3 125.5 mm to (110.4, 125.8)
- moved FB4 125.4 mm to (110.4, 127.3)
- moved C72 123.1 mm to (121.6, 124.5)
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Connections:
- C52 pad 2: /ASIC/1V2 -> /ASIC/1V2-0
- U15 pad 4: /ASIC/1V2 -> /ASIC/1V2-0
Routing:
- net /Data/SCL: track 15.8 -> 4.94 mm, vias 1 -> 0
- net /Data/SDA: track 11.7 -> 2.96 mm, vias 2 -> 1
- net /Power/PGOOD: track 12.0 -> 4.62 mm, vias 1 -> 0
- net GND: vias 33 -> 13
- added copper zone on F.Cu, net /ASIC/GND0
